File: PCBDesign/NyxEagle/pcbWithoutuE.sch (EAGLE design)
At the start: 35 parts, among them IC1 DRV8304SRHAR

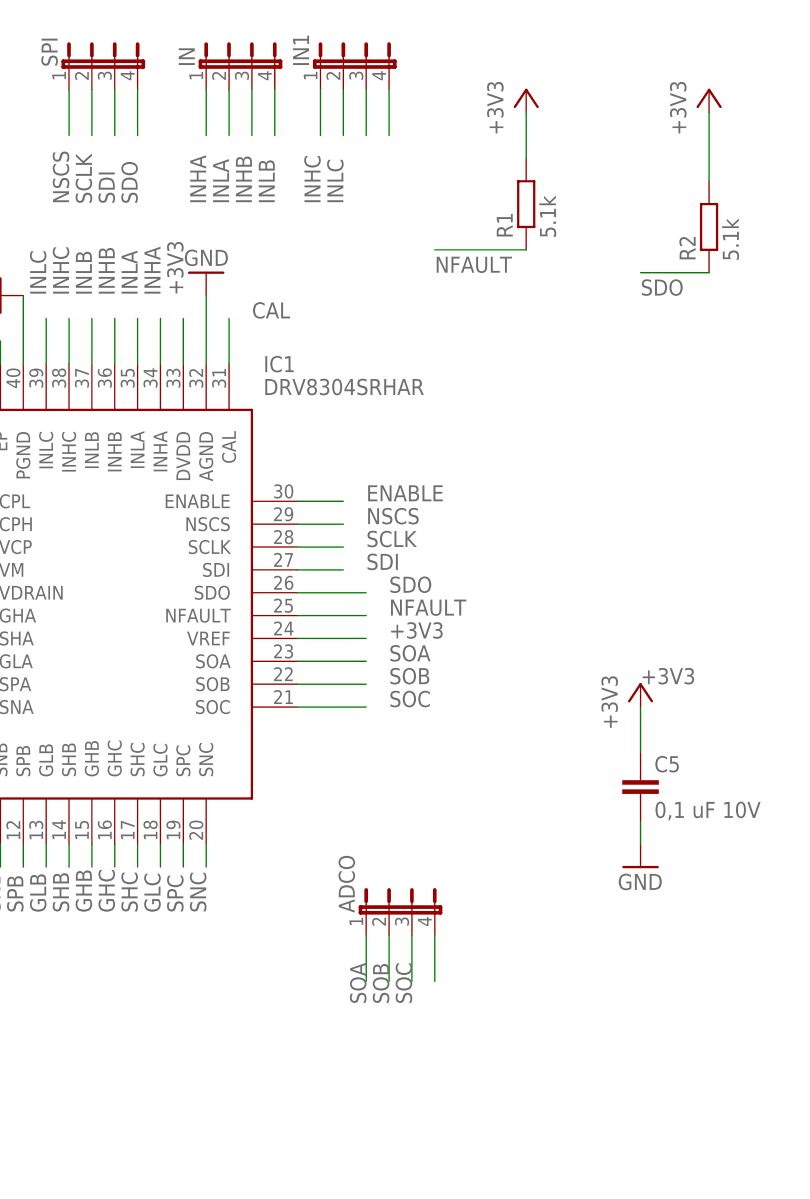
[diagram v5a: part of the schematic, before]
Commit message: PCB is ready and before the silk layer.
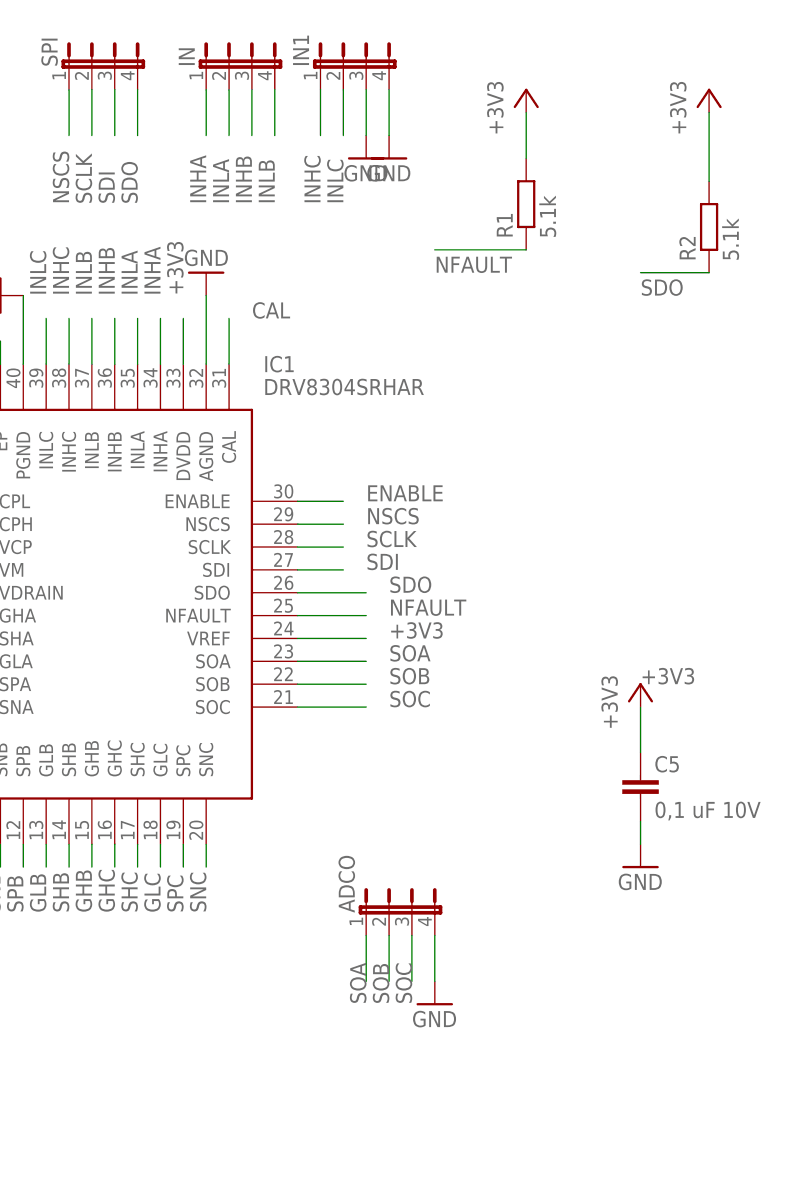
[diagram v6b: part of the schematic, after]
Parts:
- C3: device rcl:CPOL-EUE2,5-6E -> rcl:CPOL-EUE7.5-16
- GND, INPUT: device wirepad:SMD2 -> wirepad:3,17/1,3
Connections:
- removed net N$10: ADCO.4
- removed net N$6: IN1.3
- removed net N$8: IN1.4
- net GND: now also ADCO.4, IN1.3, IN1.4
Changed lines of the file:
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@@
 <part name="C1" library="rcl" library_urn="urn:adsk.eagle:library:334" deviceset="C-EU" device="C0805K" package3d_urn="urn:adsk.eagle:package:23681/2" value="22nF"/>
 <part name="C2" library="rcl" library_urn="urn:adsk.eagle:library:334" deviceset="C-EU" device="C0805K" package3d_urn="urn:adsk.eagle:package:23681/2" value="1uF 16V"/>
-<part name="C3" library="rcl" library_urn="urn:adsk.eagle:library:334" deviceset="CPOL-EU" device="E2,5-6E" package3d_urn="urn:adsk.eagle:package:23430/1" value="47uF 50V"/>
+<part name="C3" library="rcl" library_urn="urn:adsk.eagle:library:334" deviceset="CPOL-EU" device="E7.5-16" package3d_urn="urn:adsk.eagle:package:23382/2" value="47uF 50V"/>
 <part name="C4" library="rcl" library_urn="urn:adsk.eagle:library:334" deviceset="C-EU" device="C0805K" package3d_urn="urn:adsk.eagle:package:23681/2" value="0,1 uF 50V"/>
 <part name="R1" library="rcl" library_urn="urn:adsk.eagle:library:334" deviceset="R-EU_" device="R0805" package3d_urn="urn:adsk.eagle:package:23553/2" value="5.1k"/>
@@
 <part name="OUT2" library="wirepad" library_urn="urn:adsk.eagle:library:412" deviceset="SMD2" device="" package3d_urn="urn:adsk.eagle:package:30839/1"/>
 <part name="OUT3" library="wirepad" library_urn="urn:adsk.eagle:library:412" deviceset="SMD2" device="" package3d_urn="urn:adsk.eagle:package:30839/1"/>
-<part name="INPUT" library="wirepad" library_urn="urn:adsk.eagle:library:412" deviceset="SMD2" device="" package3d_urn="urn:adsk.eagle:package:30839/1"/>
-<part name="GND" library="wirepad" library_urn="urn:adsk.eagle:library:412" deviceset="SMD2" device="" package3d_urn="urn:adsk.eagle:package:30839/1"/>
+<part name="INPUT" library="wirepad" library_urn="urn:adsk.eagle:library:412" deviceset="3,17/1,3" device="" package3d_urn="urn:adsk.eagle:package:30833/1"/>
+<part name="GND" library="wirepad" library_urn="urn:adsk.eagle:library:412" deviceset="3,17/1,3" device="" package3d_urn="urn:adsk.eagle:package:30833/1"/>
 <part name="SUPPLY1" library="supply2" library_urn="urn:adsk.eagle:library:372" deviceset="AGND" device=""/>
 <part name="SUPPLY2" library="supply2" library_urn="urn:adsk.eagle:library:372" deviceset="AGND" device=""/>
@@
 <part name="R10" library="rcl" library_urn="urn:adsk.eagle:library:334" deviceset="R-EU_" device="R0201" package3d_urn="urn:adsk.eagle:package:23593/1"/>
 <part name="GND7" library="supply1" library_urn="urn:adsk.eagle:library:371" deviceset="GND" device=""/>
+<part name="GND8" library="supply1" library_urn="urn:adsk.eagle:library:371" deviceset="GND" device=""/>
+<part name="GND9" library="supply1" library_urn="urn:adsk.eagle:library:371" deviceset="GND" device=""/>
+<part name="GND10" library="supply1" library_urn="urn:adsk.eagle:library:371" deviceset="GND" device=""/>
 </parts>
 <sheets>
@@
 <instance part="R10" gate="G$1" x="142.24" y="2.54" rot="R180"/>
 <instance part="GND7" gate="1" x="-7.62" y="109.22"/>
+<instance part="GND8" gate="1" x="38.1" y="109.22"/>
+<instance part="GND9" gate="1" x="35.56" y="109.22"/>
+<instance part="GND10" gate="1" x="43.18" y="15.24"/>
 </instances>
 <busses>
@@
 <wire x1="-7.62" y1="116.84" x2="-7.62" y2="111.76" width="0.1524" layer="91"/>
 <pinref part="GND7" gate="1" pin="GND"/>
+</segment>
+<segment>
+<pinref part="IN1" gate="G$1" pin="4"/>
+<wire x1="38.1" y1="116.84" x2="38.1" y2="111.76" width="0.1524" layer="91"/>
+<pinref part="GND8" gate="1" pin="GND"/>
+</segment>
+<segment>
+<pinref part="IN1" gate="G$1" pin="3"/>
+<wire x1="35.56" y1="116.84" x2="35.56" y2="111.76" width="0.1524" layer="91"/>
+<pinref part="GND9" gate="1" pin="GND"/>
+</segment>
+<segment>
+<pinref part="ADCO" gate="G$1" pin="4"/>
+<wire x1="43.18" y1="22.86" x2="43.18" y2="17.78" width="0.1524" layer="91"/>
+<pinref part="GND10" gate="1" pin="GND"/>
 </segment>
 </net>
@@
 </segment>
 </net>
-<net name="N$6" class="0">
-<segment>
-<pinref part="IN1" gate="G$1" pin="3"/>
-<wire x1="35.56" y1="116.84" x2="35.56" y2="111.76" width="0.1524" layer="91"/>
-</segment>
-</net>
-<net name="N$8" class="0">
-<segment>
-<pinref part="IN1" gate="G$1" pin="4"/>
-<wire x1="38.1" y1="116.84" x2="38.1" y2="111.76" width="0.1524" layer="91"/>
-</segment>
-</net>
 <net name="SPA" class="0">
 <segment>
@@
 </segment>
 </net>
-<net name="N$10" class="0">
-<segment>
-<pinref part="ADCO" gate="G$1" pin="4"/>
-<wire x1="43.18" y1="22.86" x2="43.18" y2="17.78" width="0.1524" layer="91"/>
-</segment>
-</net>

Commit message: Update pcbWithoutuE.sch
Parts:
- C2: value 1uF 16V -> 1uF 50V
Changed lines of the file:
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@@
 <part name="IC1" library="SamacSys_Parts2" deviceset="DRV8304SRHAR" device=""/>
 <part name="C1" library="rcl" library_urn="urn:adsk.eagle:library:334" deviceset="C-EU" device="C0805K" package3d_urn="urn:adsk.eagle:package:23681/2" value="22nF"/>
-<part name="C2" library="rcl" library_urn="urn:adsk.eagle:library:334" deviceset="C-EU" device="C0805K" package3d_urn="urn:adsk.eagle:package:23681/2" value="1uF 16V"/>
+<part name="C2" library="rcl" library_urn="urn:adsk.eagle:library:334" deviceset="C-EU" device="C0805K" package3d_urn="urn:adsk.eagle:package:23681/2" value="1uF 50V"/>
 <part name="C3" library="rcl" library_urn="urn:adsk.eagle:library:334" deviceset="CPOL-EU" device="E7.5-16" package3d_urn="urn:adsk.eagle:package:23382/2" value="47uF 50V"/>
 <part name="C4" library="rcl" library_urn="urn:adsk.eagle:library:334" deviceset="C-EU" device="C0805K" package3d_urn="urn:adsk.eagle:package:23681/2" value="0,1 uF 50V"/>

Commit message: Update mul_s32_hiSR.h, queue.c, and 59 more files...
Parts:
- added C10, C11, C9: (no value), resistor:C-EUC0805
- added R11, R12, R13: (no value), resistor:R-EU_R0805
- added T1, T10, T11, T12, T2, T3, T4, T5, T6, T7, T8, T9: TEST_POINT1593, ERIC:TEST_POINT1593
- R10, R9: value (none) -> 0 Ohm; device rcl:R-EU_R0201 -> resistor:R-EU_R0603
- R8: value 0 -> 0 Ohm; device rcl:R-EU_R0201 -> resistor:R-EU_R0603
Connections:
- new net FED_SOA: ADCO.1, C9.1, R11.1
- new net FED_SOB: ADCO.2, C10.1, R12.2
- new net FED_SOC: ADCO.3, C11.1, R13.2
- net GHA: now also T4.1
- net GHB: now also T5.1
- net GHC: now also T6.1
- net GLA: now also T1.1
- net GLB: now also T2.1
- net GLC: now also T3.1
- net GND: now also C10.2, C11.2, C9.2
- net SHA: now also T10.1
- net SHB: now also T11.1
- net SHC: now also T12.1
- net SOA: now also R11.2; no longer ADCO.1
- net SOB: now also R12.1; no longer ADCO.2
- net SOC: now also R13.1; no longer ADCO.3
- net SPA: now also T7.1
- net SPB: now also T8.1
- net SPC: now also T9.1
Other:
- moved on the sheet: ADCO, OUT1, OUT2, OUT3, R10, R5, R8, R9
